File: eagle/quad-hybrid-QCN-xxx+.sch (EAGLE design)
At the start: 7 parts, among them J1 142-0701-851, J2 142-0701-851, J3 142-0701-851, J4 142-0701-851, U1 QCN-XXX+

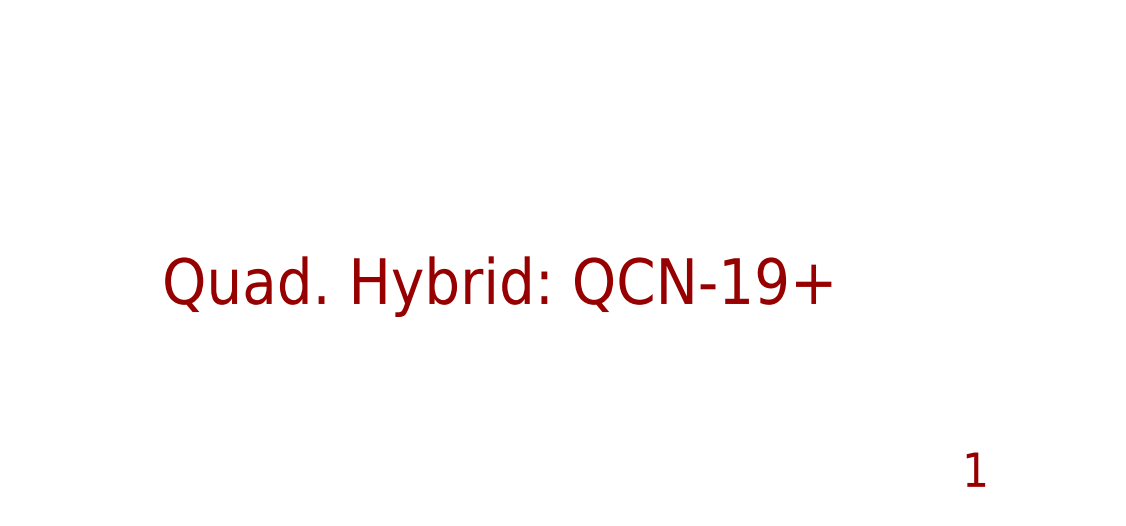
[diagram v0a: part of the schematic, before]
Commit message: Update QCN hybrid name
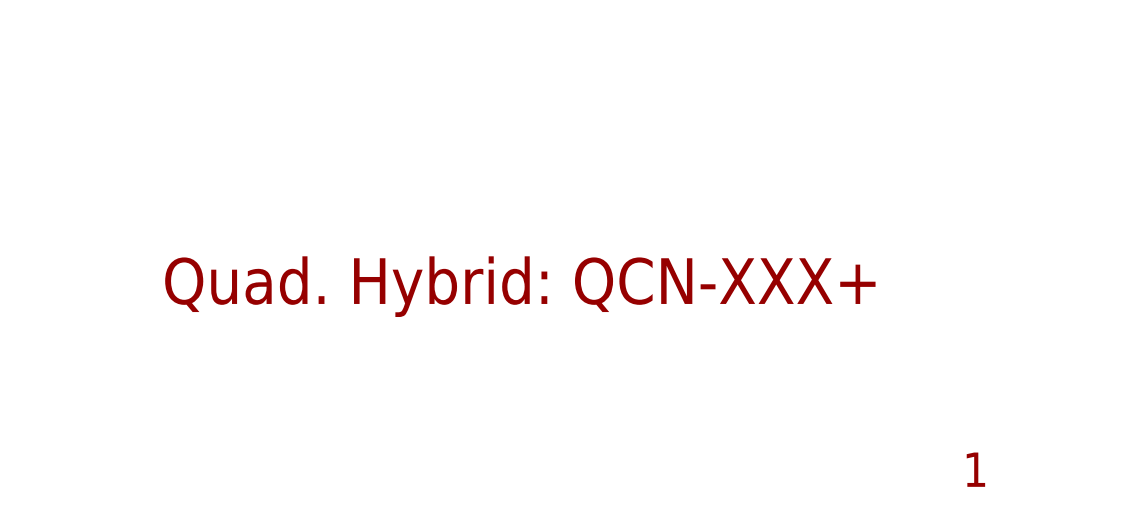
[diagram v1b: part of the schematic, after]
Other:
- note added: "Quad. Hybrid: QCN-XXX+"
- note removed: "Quad. Hybrid: QCN-19+"
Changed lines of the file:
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@@
 <sheet>
 <plain>
-<text x="176.53" y="26.67" size="5.08" layer="94">Quad. Hybrid: QCN-19+</text>
+<text x="176.53" y="26.67" size="5.08" layer="94">Quad. Hybrid: QCN-XXX+</text>
 <text x="265.43" y="6.35" size="3.81" layer="94">1</text>
 <text x="78.74" y="81.28" size="1.778" layer="97">Notes:
